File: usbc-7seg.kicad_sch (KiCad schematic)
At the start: 24 parts, among them J1 USB_C_Receptacle_USB2.0_14P, Q1 AO3400A, Q2 AO3400A, SW1 TS-1088-AR02016, U1 GS2816CX, U2 GS2816CX, U3 CH32V203GxUx, U4 XC6206P332MR-G, Y1 12MHz

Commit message: Some routing, setup board stackup properly
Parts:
- added C7: 100n, Capacitor_SMD:C_0402_1005Metric, symbol Device:C_Small
- added FB1: GZ1608D601TF, Inductor_SMD:L_0603_1608Metric, symbol Device:FerriteBead_Small
- Y1: JLCPCB Part (none) -> C9002
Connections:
- net GND: now also C7.2
- net VUSB: now also C7.1, FB1.1; no longer C1.1, U4.3 (VI)
- new net: C1.1, FB1.2, U4.3 (VI)
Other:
- moved on the sheet: C1, C2, U4

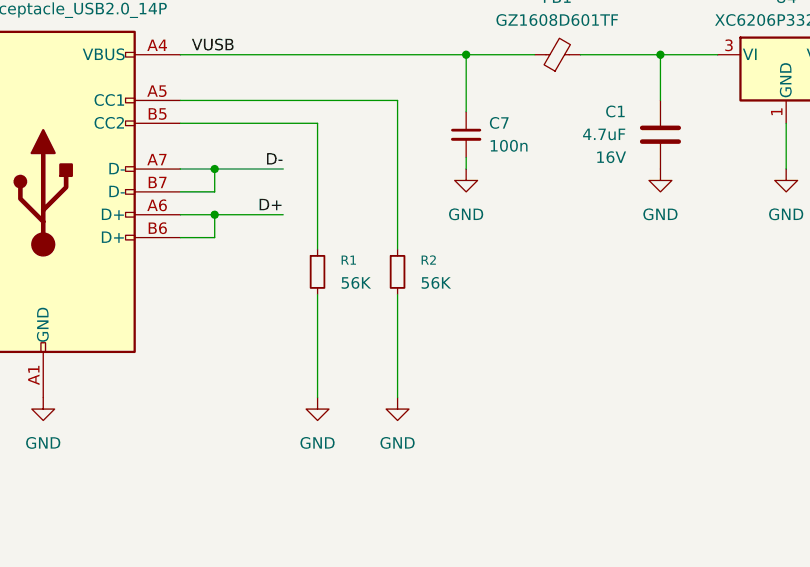
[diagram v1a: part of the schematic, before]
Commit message: Fix USB-C CC resistors
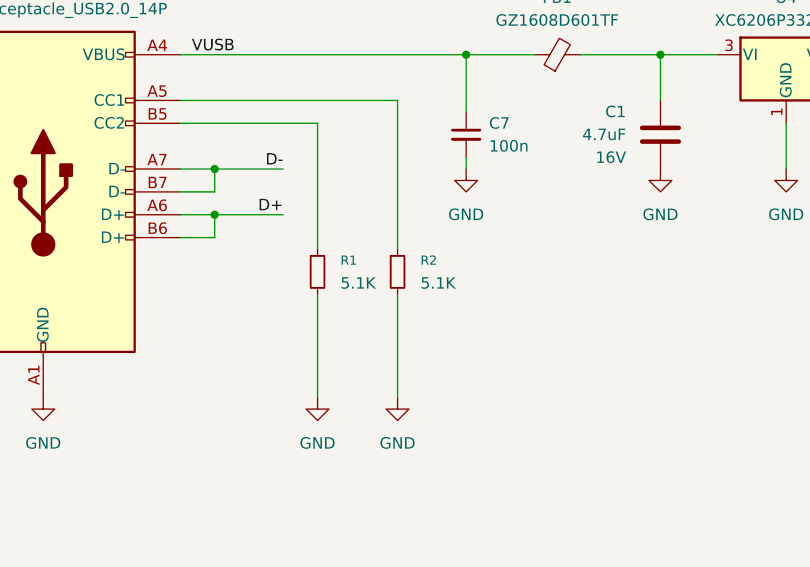
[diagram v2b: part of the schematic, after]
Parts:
- R1, R2: value 56K -> 5.1K
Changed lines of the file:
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@@
 			)
 		)
-		(property "Value" "56K"
+		(property "Value" "5.1K"
 			(at 91.44 68.5799 0)
 			(effects
@@
 			)
 		)
-		(property "Value" "56K"
+		(property "Value" "5.1K"
 			(at 82.55 68.5799 0)
 			(effects

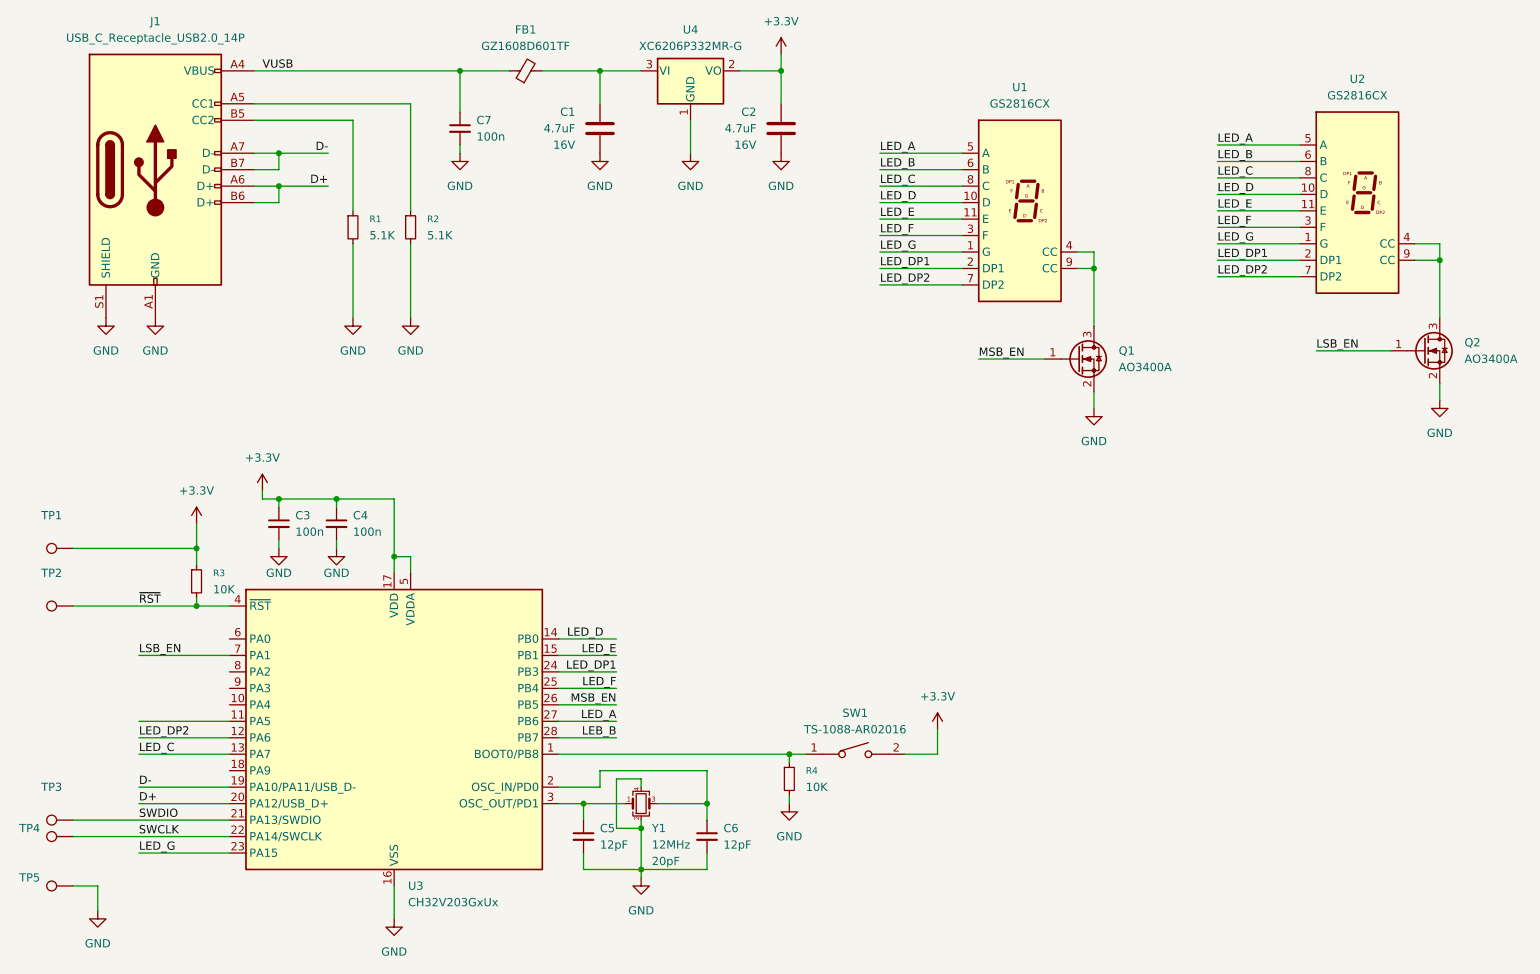
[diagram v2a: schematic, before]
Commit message: Add JLCPCB part numbers for all parts
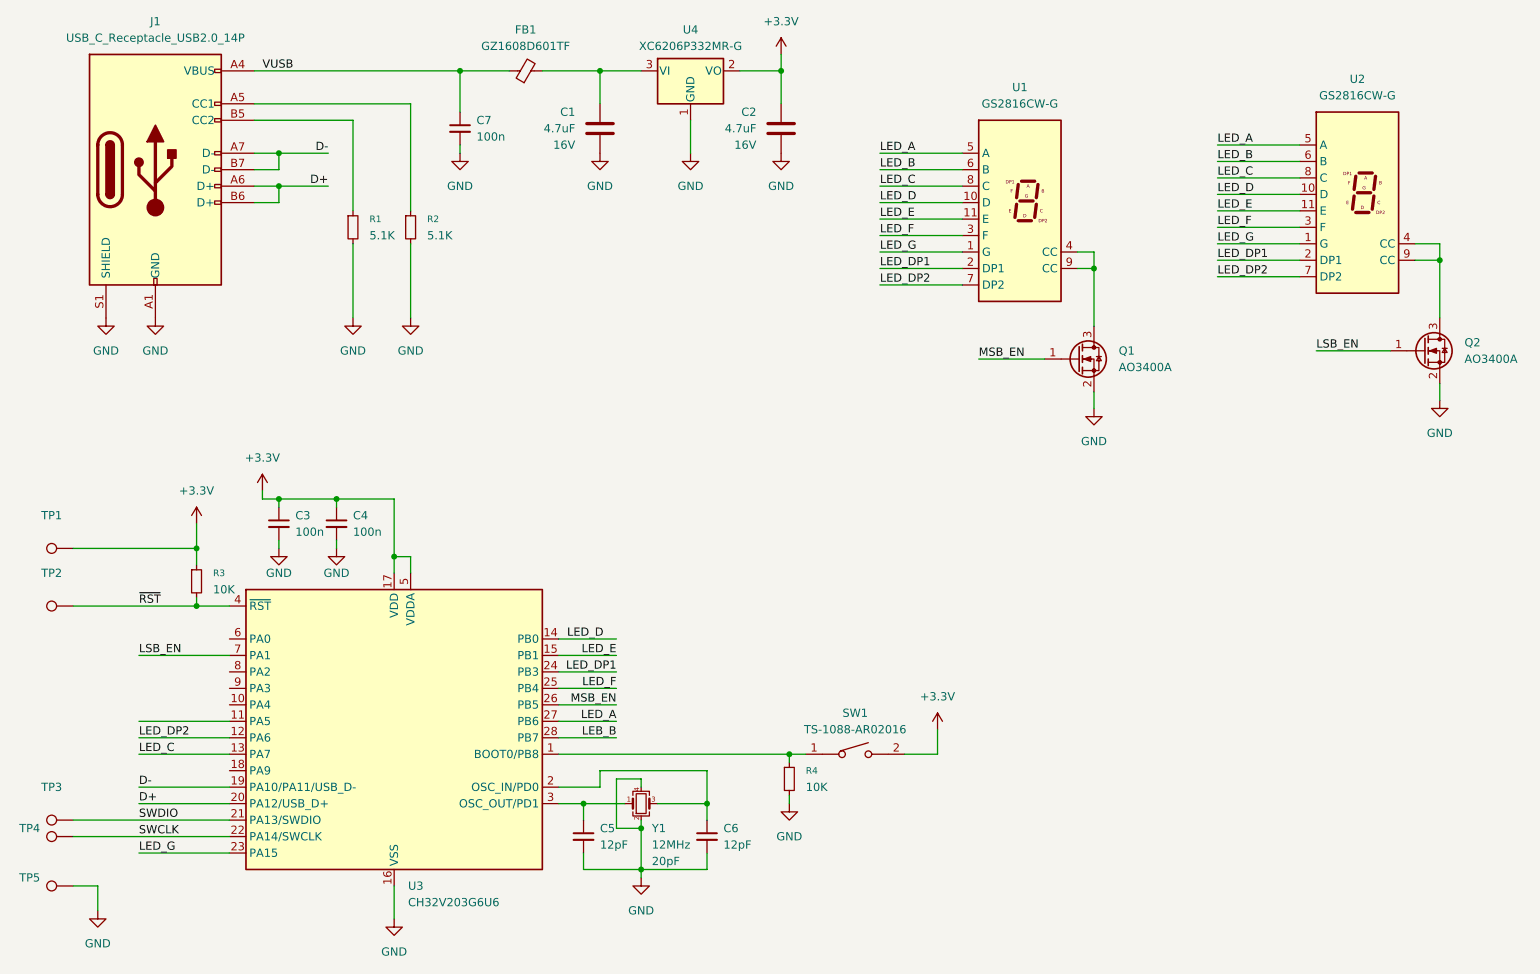
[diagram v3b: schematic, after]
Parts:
- C1, C2: JLCPCB C19666 -> (none); LCSC PN (none) -> C19666
- C3, C4, C7: LCSC PN (none) -> C1525
- C5, C6: LCSC PN (none) -> C1547
- FB1: JLCPCB Part C1002 -> (none); LCSC PN (none) -> C1002
- J1: LCSN PN (none) -> C2894897
- Q1, Q2: LCSC PN (none) -> C20917
- R1, R2: LCSC PN (none) -> C25905
- R3, R4: LCSC PN (none) -> C25744
- SW1: LCSC PN (none) -> C720477; LCSC Part C720477 -> (none)
- TP1, TP2, TP3, TP4, TP5: now left out of the parts list
- U1, U2: value GS2816CX -> GS2816CW-G; LCSC PN (none) -> C22462653
- U3: value CH32V203GxUx -> CH32V203G6U6; LCSC PN (none) -> C5142280
- U4: LCSC PN (none) -> C5446; LCSC Part C5446 -> (none)
- Y1: JLCPCB Part C9002 -> (none); LCSC PN (none) -> C9002
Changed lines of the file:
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@@
 			)
 		)
+		(property "LCSC PN" "C25905"
+			(at 88.9 67.31 0)
+			(effects
+				(font
+					(size 1.27 1.27)
+				)
+				(hide yes)
+			)
+		)
 		(pin "2"
 		)
@@
 			)
 		)
+		(property "LCSC PN" "C1547"
+			(at 134.62 161.29 0)
+			(effects
+				(font
+					(size 1.27 1.27)
+				)
+				(hide yes)
+			)
+		)
 		(pin "1"
 		)
@@
 			)
 		)
+		(property "LCSC PN" "C25905"
+			(at 80.01 67.31 0)
+			(effects
+				(font
+					(size 1.27 1.27)
+				)
+				(hide yes)
+			)
+		)
 		(pin "1"
 		)
@@
 			)
 		)
-		(property "JLCPCB" "C19666"
+		(property "LCSC PN" "C19666"
 			(at 118.11 52.07 0)
 			(effects
@@
 			)
 		)
+		(property "LCSN PN" "C2894897"
+			(at 49.53 58.42 0)
+			(effects
+				(font
+					(size 1.27 1.27)
+				)
+				(hide yes)
+			)
+		)
 		(pin "S1"
 		)
@@
 			)
 		)
-		(property "JLCPCB Part" "C1002"
+		(property "LCSC PN" "C1002"
 			(at 106.68 43.18 90)
 			(effects
@@
 			)
 		)
+		(property "LCSC PN" "C20917"
+			(at 191.77 87.63 0)
+			(effects
+				(font
+					(size 1.27 1.27)
+				)
+				(hide yes)
+			)
+		)
 		(pin "3"
 		)
@@
 			)
 		)
-		(property "JLCPCB Part" "C9002"
+		(property "LCSC PN" "C9002"
 			(at 124.46 156.21 0)
 			(effects
@@
 			)
 		)
-		(property "Value" "GS2816CX"
+		(property "Value" "GS2816CW-G"
 			(at 234.95 46.99 0)
 			(effects
@@
 			)
 		)
+		(property "LCSC PN" "C22462653"
+			(at 234.95 62.23 0)
+			(effects
+				(font
+					(size 1.27 1.27)
+				)
+				(hide yes)
+			)
+		)
 		(pin "2"
 		)
@@
 			)
 		)
+		(property "LCSC PN" "C20917"
+			(at 245.11 86.36 0)
+			(effects
+				(font
+					(size 1.27 1.27)
+				)
+				(hide yes)
+			)
+		)
 		(pin "3"
 		)
@@
 			)
 		)
+		(property "LCSC PN" "C1525"
+			(at 68.58 113.03 0)
+			(effects
+				(font
+					(size 1.27 1.27)
+				)
+				(hide yes)
+			)
+		)
 		(pin "2"
 		)
@@
 			)
 		)
-		(property "Value" "CH32V203GxUx"
+		(property "Value" "CH32V203G6U6"
 			(at 88.5033 171.45 0)
 			(effects
@@
 			)
 		)
+		(property "LCSC PN" "C5142280"
+			(at 86.36 146.05 0)
+			(effects
+				(font
+					(size 1.27 1.27)
+				)
+				(hide yes)
+			)
+		)
 		(pin "29"
 		)
@@
 		(unit 1)
 		(exclude_from_sim no)
-		(in_bom yes)
+		(in_bom no)
 		(on_board yes)
 		(dnp no)
@@
 			)
 		)
+		(property "LCSC PN" "C1547"
+			(at 115.57 161.29 0)
+			(effects
+				(font
+					(size 1.27 1.27)
+				)
+				(hide yes)
+			)
+		)
 		(pin "1"
 		)
@@
 			)
 		)
+		(property "LCSC PN" "C25744"
+			(at 147.32 152.4 0)
+			(effects
+				(font
+					(size 1.27 1.27)
+				)
+				(hide yes)
+			)
+		)
 		(pin "2"
 		)
@@
 		(unit 1)
 		(exclude_from_sim no)
-		(in_bom yes)
+		(in_bom no)
 		(on_board yes)
 		(dnp no)
@@
 			)
 		)
+		(property "LCSC PN" "C1525"
+			(at 77.47 113.03 0)
+			(effects
+				(font
+					(size 1.27 1.27)
+				)
+				(hide yes)
+			)
+		)
 		(pin "2"
 		)
@@
 			)
 		)
+		(property "LCSC PN" "C25744"
+			(at 55.88 121.92 0)
+			(effects
+				(font
+					(size 1.27 1.27)
+				)
+				(hide yes)
+			)
+		)
 		(pin "2"
 		)
@@
 			)
 		)
-		(property "LCSC Part" "C5446"
+		(property "LCSC PN" "C5446"
 			(at 132.08 43.18 0)
 			(effects
@@
 			)
 		)
-		(property "Value" "GS2816CX"
+		(property "Value" "GS2816CW-G"
 			(at 182.88 48.26 0)
 			(effects
@@
 			)
 		)
+		(property "LCSC PN" "C22462653"
+			(at 182.88 63.5 0)
+			(effects
+				(font
+					(size 1.27 1.27)
+				)
+				(hide yes)
+			)
+		)
 		(pin "2"
 		)
@@
 		(unit 1)
 		(exclude_from_sim no)
-		(in_bom yes)
+		(in_bom no)
 		(on_board yes)
 		(dnp no)
@@
 			)
 		)
+		(property "LCSC PN" "C1525"
+			(at 96.52 52.07 0)
+			(effects
+				(font
+					(size 1.27 1.27)
+				)
+				(hide yes)
+			)
+		)
 		(pin "2"
 		)
@@
 			)
 		)
-		(property "LCSC Part" "C720477"
+		(property "LCSC PN" "C720477"
 			(at 157.48 161.29 0)
 			(effects
@@
 		(unit 1)
 		(exclude_from_sim no)
-		(in_bom yes)
+		(in_bom no)
 		(on_board yes)
 		(dnp no)
@@
 		(unit 1)
 		(exclude_from_sim no)
-		(in_bom yes)
+		(in_bom no)
 		(on_board yes)
 		(dnp no)
@@
 			)
 		)
-		(property "JLCPCB" "C19666"
+		(property "LCSC PN" "C19666"
 			(at 146.05 52.07 0)
 			(effects
